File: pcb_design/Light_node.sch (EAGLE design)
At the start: 27 parts, among them IC1 ATmega328P, IC2 MIC5225-5v, Q1 reset, Y1 16MHz

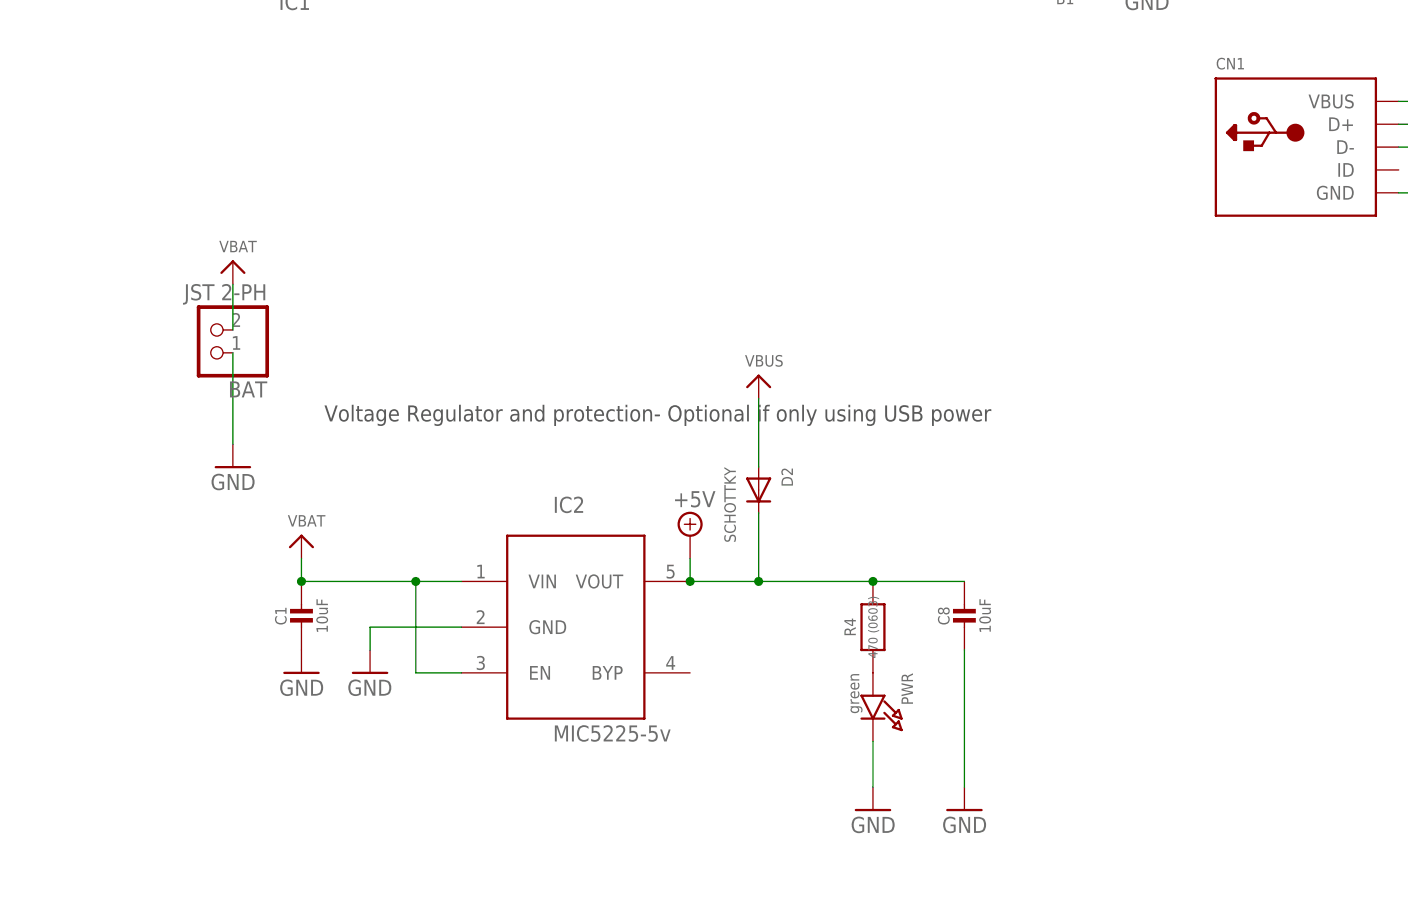
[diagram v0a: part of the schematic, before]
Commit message: Pulled the regulator components
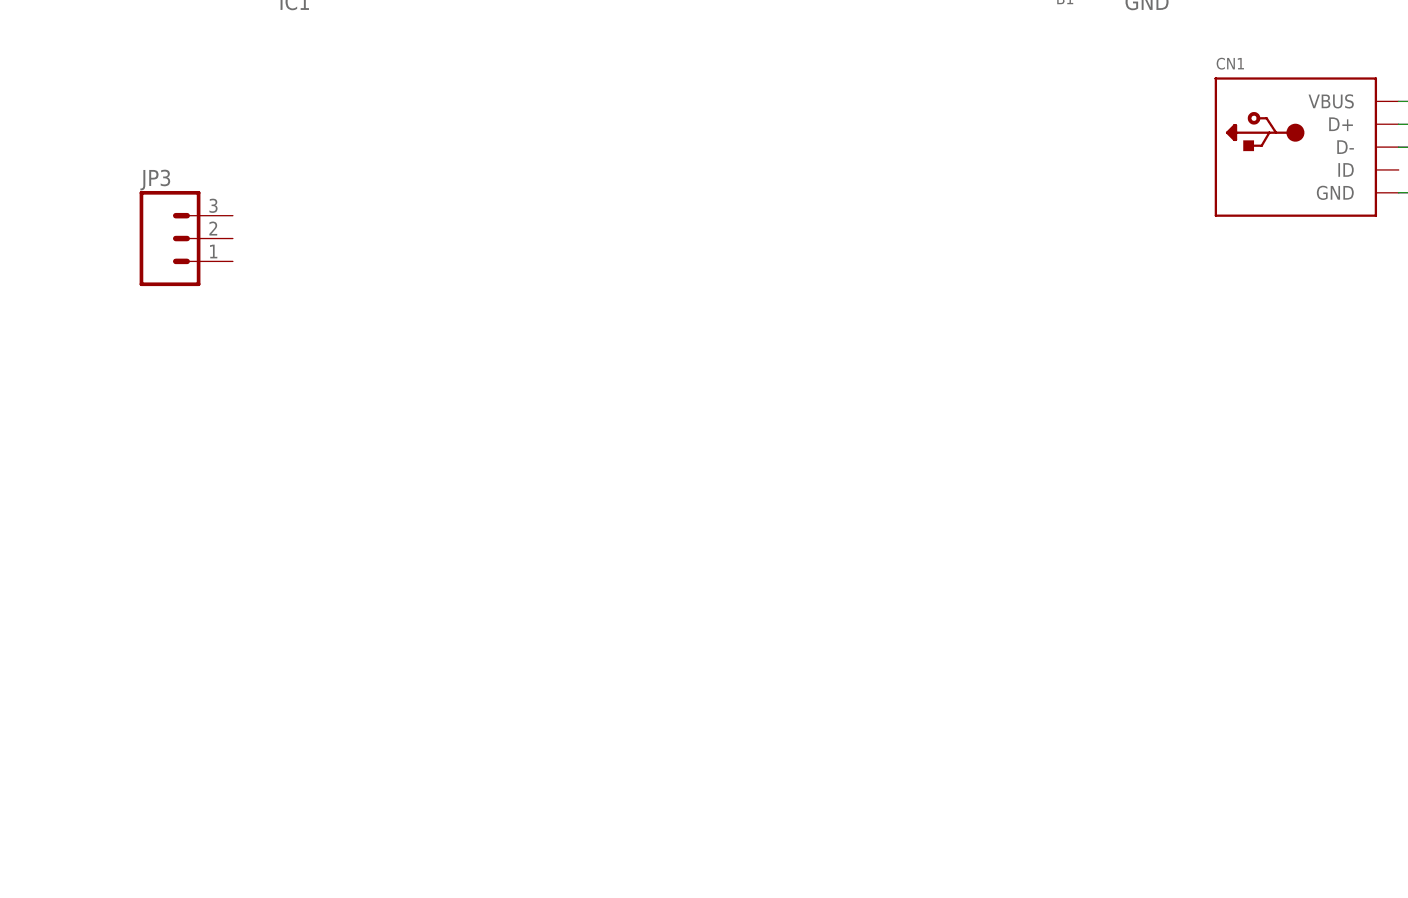
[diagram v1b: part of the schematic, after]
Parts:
- removed BAT: JST 2-PH, microbuilder:CON_JST_PH_2PIN
- removed C1, C8: 10uF, microbuilder:CAP_CERAMIC0805-NOOUTLINE
- removed D2: SCHOTTKY, adafruit:DIODE_SOD-123FL
- removed IC2: MIC5225-5v, adafruit:LP298XS
- removed PWR: green, microbuilder:LED0805_NOOUTLINE
- removed R4: 470 (0603), microbuilder:RESISTOR_0603_NOOUT
- added JP3: (no value), SparkFun:M03JST-PTH
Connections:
- removed net N$6: PWR.A, R4.1
- net +5V: no longer C8.1, D2.C, IC2.VOUT, R4.2
- net GND: no longer BAT.1, C1.2, C8.2, IC2.GND, PWR.C
- net VBAT: no longer BAT.2, C1.1, IC2.EN, IC2.VIN
- net VBUS: no longer D2.A
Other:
- note removed: "Voltage Regulator and protection- Optional if only using USB power"
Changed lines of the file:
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@@
 <part name="R2" library="microbuilder" deviceset="RESISTOR" device="_0603_NOOUT" value="68 (0603)"/>
 <part name="GND1" library="supply1" deviceset="GND" device=""/>
-<part name="GND12" library="supply1" deviceset="GND" device=""/>
 <part name="U$1" library="adafruit" deviceset="FIDUCIAL" device=""/>
 <part name="U$6" library="adafruit" deviceset="FIDUCIAL" device=""/>
 <part name="FRAME1" library="frames" deviceset="FRAME_A_L" device=""/>
-<part name="IC2" library="adafruit" deviceset="LP298X" device="S" value="MIC5225-5v"/>
-<part name="GND11" library="supply1" deviceset="GND" device=""/>
-<part name="C8" library="microbuilder" deviceset="CAP_CERAMIC" device="0805-NOOUTLINE" value="10uF"/>
 <part name="R3" library="microbuilder" deviceset="RESISTOR" device="_0603_NOOUT" value="1.5K (0603)"/>
 <part name="GND5" library="supply1" deviceset="GND" device=""/>
 <part name="Q1" library="microbuilder" deviceset="SWITCH_TACT_SMT" device="4.6X2.8" value="reset"/>
-<part name="R4" library="microbuilder" deviceset="RESISTOR" device="_0603_NOOUT" value="470 (0603)"/>
-<part name="PWR" library="microbuilder" deviceset="LED" device="0805_NOOUTLINE" value="green"/>
-<part name="GND6" library="supply1" deviceset="GND" device=""/>
-<part name="D2" library="adafruit" deviceset="DIODE" device="_SOD-123FL" value="SCHOTTKY"/>
-<part name="U$3" library="microbuilder" deviceset="VBUS" device=""/>
-<part name="U$4" library="microbuilder" deviceset="VBAT" device=""/>
-<part name="C1" library="microbuilder" deviceset="CAP_CERAMIC" device="0805-NOOUTLINE" value="10uF"/>
-<part name="GND3" library="supply1" deviceset="GND" device=""/>
 <part name="R5" library="microbuilder" deviceset="RESISTOR" device="_0603_NOOUT" value="470 (0603)"/>
 <part name="B1" library="microbuilder" deviceset="LED" device="0805_NOOUTLINE" value="red"/>
@@
 <part name="JP2" library="microbuilder" deviceset="HEADER-1X2" device="ROUND"/>
 <part name="GND13" library="supply1" deviceset="GND" device=""/>
-<part name="BAT" library="microbuilder" deviceset="CON_JST_PH_2PIN" device="" value="JST 2-PH"/>
-<part name="U$8" library="microbuilder" deviceset="VBAT" device=""/>
-<part name="GND16" library="supply1" deviceset="GND" device=""/>
 <part name="D1" library="microbuilder" deviceset="DIODE" device="SOD-323" value="3.6v"/>
 <part name="D4" library="microbuilder" deviceset="DIODE" device="SOD-323" value="3.6V"/>
@@
 <part name="GND15" library="supply1" deviceset="GND" device=""/>
 <part name="SUPPLY1" library="supply2" deviceset="+5V" device=""/>
-<part name="SUPPLY3" library="supply2" deviceset="+5V" device=""/>
 <part name="SUPPLY4" library="supply2" deviceset="+5V" device=""/>
 <part name="SUPPLY5" library="supply2" deviceset="+5V" device=""/>
 <part name="SUPPLY6" library="supply2" deviceset="+5V" device=""/>
 <part name="SUPPLY7" library="supply2" deviceset="+5V" device=""/>
+<part name="JP3" library="SparkFun" deviceset="M03" device="JST-PTH"/>
 </parts>
 <sheets>
@@
 <text x="175.26" y="25.4" size="2.54" layer="94">http://adafruit.com/products/2000</text>
 <text x="248.92" y="30.48" size="2.54" layer="94">CC 2.5 BY-SA</text>
-<text x="50.8" y="58.42" size="1.778" layer="97">Voltage Regulator and protection- Optional if only using USB power</text>
 </plain>
 <instances>
@@
 <instance part="R2" gate="G$1" x="193.04" y="86.36"/>
 <instance part="GND1" gate="1" x="177.8" y="78.74"/>
-<instance part="GND12" gate="1" x="121.92" y="15.24" rot="MR0"/>
 <instance part="U$1" gate="G$1" x="246.38" y="10.16"/>
 <instance part="U$6" gate="G$1" x="241.3" y="10.16"/>
 <instance part="FRAME1" gate="G$1" x="0" y="0"/>
 <instance part="FRAME1" gate="G$2" x="172.72" y="0"/>
-<instance part="IC2" gate="G$1" x="81.28" y="35.56" rot="R270"/>
-<instance part="GND11" gate="1" x="55.88" y="30.48"/>
-<instance part="C8" gate="G$1" x="121.92" y="35.56"/>
 <instance part="R3" gate="G$1" x="187.96" y="99.06" rot="R90"/>
 <instance part="GND5" gate="1" x="48.26" y="195.58" rot="MR270"/>
 <instance part="Q1" gate="G$1" x="40.64" y="195.58"/>
-<instance part="R4" gate="G$1" x="111.76" y="35.56" rot="R90"/>
-<instance part="PWR" gate="G$1" x="111.76" y="25.4" rot="R270"/>
-<instance part="GND6" gate="1" x="111.76" y="15.24" rot="MR0"/>
-<instance part="D2" gate="G$1" x="99.06" y="50.8" rot="R270"/>
-<instance part="U$3" gate="G$1" x="99.06" y="63.5"/>
-<instance part="U$4" gate="G$1" x="48.26" y="45.72"/>
-<instance part="C1" gate="G$1" x="48.26" y="35.56"/>
-<instance part="GND3" gate="1" x="48.26" y="30.48" rot="MR0"/>
 <instance part="R5" gate="G$1" x="124.46" y="109.22" rot="MR0"/>
 <instance part="B1" gate="G$1" x="137.16" y="109.22" rot="MR180"/>
@@
 <instance part="JP2" gate="G$1" x="104.14" y="149.86"/>
 <instance part="GND13" gate="1" x="40.64" y="119.38"/>
-<instance part="BAT" gate="G$1" x="38.1" y="68.58" rot="R180"/>
-<instance part="U$8" gate="G$1" x="40.64" y="76.2"/>
-<instance part="GND16" gate="1" x="40.64" y="53.34" rot="MR0"/>
 <instance part="D1" gate="G$1" x="182.88" y="83.82" rot="R90"/>
 <instance part="D4" gate="G$1" x="193.04" y="81.28" rot="R90"/>
@@
 <instance part="GND15" gate="1" x="193.04" y="76.2"/>
 <instance part="SUPPLY1" gate="+5V" x="22.86" y="180.34"/>
-<instance part="SUPPLY3" gate="+5V" x="91.44" y="45.72"/>
 <instance part="SUPPLY4" gate="+5V" x="187.96" y="106.68"/>
 <instance part="SUPPLY5" gate="+5V" x="33.02" y="157.48" rot="R90"/>
 <instance part="SUPPLY6" gate="+5V" x="38.1" y="129.54" rot="R90"/>
 <instance part="SUPPLY7" gate="+5V" x="157.48" y="185.42" rot="R90"/>
+<instance part="JP3" gate="G$1" x="33.02" y="78.74"/>
 </instances>
 <busses>
@@
 </segment>
 <segment>
-<wire x1="121.92" y1="17.78" x2="121.92" y2="33.02" width="0.1524" layer="91"/>
-<pinref part="GND12" gate="1" pin="GND"/>
-<pinref part="C8" gate="G$1" pin="2"/>
-</segment>
-<segment>
-<wire x1="66.04" y1="35.56" x2="55.88" y2="35.56" width="0.1524" layer="91"/>
-<wire x1="55.88" y1="35.56" x2="55.88" y2="33.02" width="0.1524" layer="91"/>
-<pinref part="GND11" gate="1" pin="GND"/>
-<pinref part="IC2" gate="G$1" pin="GND"/>
-</segment>
-<segment>
 <wire x1="45.72" y1="193.04" x2="45.72" y2="195.58" width="0.1524" layer="91"/>
 <pinref part="GND5" gate="1" pin="GND"/>
@@
 <junction x="45.72" y="195.58"/>
 <pinref part="Q1" gate="G$1" pin="S1"/>
-</segment>
-<segment>
-<pinref part="PWR" gate="G$1" pin="C"/>
-<pinref part="GND6" gate="1" pin="GND"/>
-<wire x1="111.76" y1="17.78" x2="111.76" y2="22.86" width="0.1524" layer="91"/>
-</segment>
-<segment>
-<pinref part="C1" gate="G$1" pin="2"/>
-<pinref part="GND3" gate="1" pin="GND"/>
 </segment>
 <segment>
@@
 <pinref part="IC1" gate="G$1" pin="THERMAL"/>
 <pinref part="GND13" gate="1" pin="GND"/>
-</segment>
-<segment>
-<pinref part="BAT" gate="G$1" pin="1"/>
-<pinref part="GND16" gate="1" pin="GND"/>
-<wire x1="40.64" y1="55.88" x2="40.64" y2="66.04" width="0.1524" layer="91"/>
 </segment>
 <segment>
@@
 <net name="VBUS" class="1">
 <segment>
-<pinref part="U$3" gate="G$1" pin="VBUS"/>
-<wire x1="99.06" y1="53.34" x2="99.06" y2="60.96" width="0.1524" layer="91"/>
-<pinref part="D2" gate="G$1" pin="A"/>
-</segment>
-<segment>
 <pinref part="CN1" gate="G$1" pin="VBUS"/>
 <pinref part="U$2" gate="G$1" pin="VBUS"/>
@@
 </segment>
 </net>
-<net name="N$6" class="0">
-<segment>
-<pinref part="R4" gate="G$1" pin="1"/>
-<pinref part="PWR" gate="G$1" pin="A"/>
-</segment>
-</net>
 <net name="VBAT" class="1">
-<segment>
-<pinref part="U$4" gate="G$1" pin="VBAT"/>
-<wire x1="48.26" y1="40.64" x2="48.26" y2="43.18" width="0.1524" layer="91"/>
-<wire x1="60.96" y1="40.64" x2="66.04" y2="40.64" width="0.1524" layer="91"/>
-<wire x1="66.04" y1="30.48" x2="60.96" y2="30.48" width="0.1524" layer="91"/>
-<wire x1="60.96" y1="30.48" x2="60.96" y2="40.64" width="0.1524" layer="91"/>
-<junction x="60.96" y="40.64"/>
-<pinref part="IC2" gate="G$1" pin="VIN"/>
-<pinref part="IC2" gate="G$1" pin="EN"/>
-<pinref part="C1" gate="G$1" pin="1"/>
-<junction x="48.26" y="40.64"/>
-<wire x1="48.26" y1="40.64" x2="60.96" y2="40.64" width="0.1524" layer="91"/>
-</segment>
 <segment>
 <wire x1="172.72" y1="193.04" x2="160.02" y2="193.04" width="0.1524" layer="91"/>
 <label x="160.02" y="193.04" size="1.778" layer="95"/>
 <pinref part="JP1" gate="G$1" pin="1"/>
-</segment>
-<segment>
-<pinref part="U$8" gate="G$1" pin="VBAT"/>
-<pinref part="BAT" gate="G$1" pin="2"/>
-<wire x1="40.64" y1="68.58" x2="40.64" y2="73.66" width="0.1524" layer="91"/>
 </segment>
 </net>
@@
 </segment>
 <segment>
-<pinref part="IC2" gate="G$1" pin="VOUT"/>
-<wire x1="91.44" y1="43.18" x2="91.44" y2="40.64" width="0.1524" layer="91"/>
-<wire x1="91.44" y1="40.64" x2="99.06" y2="40.64" width="0.1524" layer="91"/>
-<junction x="91.44" y="40.64"/>
-<pinref part="R4" gate="G$1" pin="2"/>
-<pinref part="C8" gate="G$1" pin="1"/>
-<wire x1="99.06" y1="40.64" x2="111.76" y2="40.64" width="0.1524" layer="91"/>
-<wire x1="111.76" y1="40.64" x2="121.92" y2="40.64" width="0.1524" layer="91"/>
-<junction x="111.76" y="40.64"/>
-<pinref part="SUPPLY3" gate="+5V" pin="+5V"/>
-<pinref part="D2" gate="G$1" pin="C"/>
-<wire x1="99.06" y1="48.26" x2="99.06" y2="40.64" width="0.1524" layer="91"/>
-<junction x="99.06" y="40.64"/>
-</segment>
-<segment>

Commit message: added a bunch of new stuff in
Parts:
- removed JP2: (no value), microbuilder:HEADER-1X2ROUND
- removed JP4: (no value), adafruit:PINHD-1X12-CB
- added B2: red, microbuilder:LED0805_NOOUTLINE
- added C1, C4: 10µF, microbuilder:CAP_CERAMIC0805-NOOUTLINE
- added C5, C8: 10uF, microbuilder:CAP_CERAMIC0805-NOOUTLINE
- added CN2: JSTPH, microbuilder:JST_2PIN
- added D2, D3: SCHOTTKY, adafruit:DIODE_SOD-123FL
- added IC2: MIC5225-3.3v, adafruit:LP298XS
- added LED2: GREEN, microbuilder:LED0805_NOOUTLINE
- added R4: 470 (0603), microbuilder:RESISTOR_0603_NOOUT
- added R8: 470, microbuilder:RESISTOR0805_NOOUTLINE
- added R9: 10K\, microbuilder:RESISTOR0805_NOOUTLINE
- added U1: MCP73831T-2ACI/OT, microbuilder:MCP73831/2
- JP1: device adafruit:PINHD-1X12-CB -> microbuilder:HEADER-1X2ROUND
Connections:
- new net +3V3: C8.1, IC2.VOUT
- new net N$10: IC1.VCC@1, IC1.VCC@2
- new net N$4: B2.A, R4.1
- new net N$5: IC1.AVCC
- new net N$6: R8.2, U1.STAT
- new net N$7: R9.1, U1.PROG
- new net N$8: LED2.A, R8.1
- new net N$9: C5.1, D2.C, D3.C, IC2.EN, IC2.VIN
- new net STRIP_CNTRL: JP3.2
- net +5V: now also C1.1, CN1.VBUS, D2.A, JP1.1, R4.2, U1.VDD; no longer IC1.AVCC, IC1.VCC@1, IC1.VCC@2, JP1.4, R6.2
- net A0: no longer JP4.7
- net A1: no longer JP4.8
- net A2: no longer JP4.9
- net A3: no longer JP4.10
- net A4: no longer JP4.11
- net A5: no longer JP4.12
- net A6: no longer JP2.1
- net A7: no longer JP2.2
- net AREF: no longer JP4.6
- net D10: no longer JP4.2
- net D11: no longer JP4.3
- net D12: no longer JP4.4
- net D13: no longer JP4.5
- net D3: no longer JP1.9
- net D4: no longer JP1.8
- net D5: no longer JP1.7
- net D6: no longer JP1.6
- net D8: no longer JP1.5
- net D9: no longer JP4.1
- net GND: now also B2.C, C1.2, C4.2, C5.2, C8.2, CN2.1, IC2.GND, JP3.1, LED2.C, R9.2, U1.VSS; no longer JP1.2
- net RESET: no longer JP1.12
- net RXD: no longer JP1.11
- net TXD: no longer JP1.10
- net VBAT: now also C4.1, CN2.2, D3.A, JP1.2, JP3.3, U1.VBAT; no longer JP1.1
- net VBUS: no longer CN1.VBUS, JP1.3
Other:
- note added: "1.0K = 1000mA"
- note added: "10K = 100mA"
- note added: "2.0K = 500mA"
- note added: "5.0K = 200mA"
- note added: "Assembly and use note : If you plan to do USB-powered operation, do not populate the Battery Charge electronics. Instead you need to solder JP1 shut"
- note added: "Battery Charger Circuit"
- note added: "USB Data and Power In"
- note added: "USB power LED"
- moved on the sheet: B1, CN1, D1, D4, R1, R2, R3, R5

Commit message: jumpe us over to using the 3.3V version of the promicro
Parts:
- removed CN2: JSTPH, microbuilder:JST_2PIN
- removed D1: 3.6v, microbuilder:DIODESOD-323
- removed D4: 3.6V, microbuilder:DIODESOD-323
- removed R8: 470, microbuilder:RESISTOR0805_NOOUTLINE
- removed R9: 10K\, microbuilder:RESISTOR0805_NOOUTLINE
- added CN3: JSTPH, microbuilder:JST_2PIN
- added JP2, JP5: (no value), microbuilder:HEADER-1X2ROUND
- added JP4: (no value), adafruit:PINHD-1X12-CB
- added PWR: green, microbuilder:LED0805_NOOUTLINE
- added R10: 470 (0603), microbuilder:RESISTOR_0603_NOOUT
- added R11: 470, microbuilder:RESISTOR0805_NOOUTLINE
- added R12: 10K\, microbuilder:RESISTOR0805_NOOUTLINE
- C1: value 10µF -> 10uF
- C5: value 10uF -> 10µF
- JP1: device microbuilder:HEADER-1X2ROUND -> adafruit:PINHD-1X12-CB
- R6: value 10K -> 10K (0603)
- Y1: value 16MHz -> 12MHz
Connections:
- removed net N$10: IC1.VCC@1, IC1.VCC@2
- net +3V3: now also IC1.AVCC, IC1.VCC@1, IC1.VCC@2, JP1.4, R3.2, R4.2, R6.2
- net +5V: now also C4.1, JP5.1, R10.2; no longer C1.1, JP1.1, R3.2, R4.2
- net A0: now also JP4.7
- net A1: now also JP4.8
- net A2: now also JP4.9
- net A3: now also JP4.10
- net A4: now also JP4.11
- net A5: now also JP4.12
- net A6: now also JP2.1
- net A7: now also JP2.2
- net AREF: now also JP4.6
- net D+: no longer D1.C
- net D-: no longer D4.C
- net D10: now also JP4.2
- net D11: now also JP4.3
- net D12: now also JP4.4
- net D13: now also JP4.5
- net D3: now also JP1.9
- net D4: now also JP1.8
- net D5: now also JP1.7
- net D6: now also JP1.6
- net D8: now also JP1.5
- net D9: now also JP4.1
- net GND: now also CN3.1, JP1.2, PWR.C, R12.2; no longer CN2.1, D1.A, D4.A, R9.2
- net N$4: now also R10.1; no longer R4.1
- net N$5: now also R11.2, U1.STAT; no longer IC1.AVCC
- net N$6: now also PWR.A, R4.1; no longer R8.2, U1.STAT
- net N$7: now also C1.1, D2.C, D3.C, IC2.EN, IC2.VIN; no longer R9.1, U1.PROG
- net N$8: now also R12.1, U1.PROG; no longer LED2.A, R8.1
- net N$9: now also LED2.A, R11.1; no longer C5.1, D2.C, D3.C, IC2.EN, IC2.VIN
- net RESET: now also JP1.12
- net RXD: now also JP1.11
- net TXD: now also JP1.10
- net VBAT: now also C5.1, CN3.2, JP1.1, JP5.2; no longer C4.1, CN2.2, JP1.2
- net VBUS: now also JP1.3
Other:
- note added: "Adafruit Pro Trinket 3.3V"
- note added: "http://adafruit.com/products/2010"
- note removed: "Adafruit Pro Trinket 5V"
- note removed: "Assembly and use note : If you plan to do USB-powered operation, do not populate the Battery Charge electronics. Instead you need to solder JP1 shut"
- note removed: "USB Data and Power In"
- note removed: "http://adafruit.com/products/2000"
- moved on the sheet: B1, B2, C1, C4, C5, C8, CN1, D2, D3, IC2, JP3, LED2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

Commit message: added in the accelerometer and removed the Reset pin
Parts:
- removed Q1: reset, microbuilder:SWITCH_TACT_SMT4.6X2.8
- added C6: 0.1uF, microbuilder:CAP_CERAMIC0805_10MGAP
- added C7: 10µF, microbuilder:CAP_CERAMIC0805-NOOUTLINE
- added JP6: (no value), microbuilder:HEADER-1X3ROUND
- added R16, R8: 10K, microbuilder:RESISTOR0805_NOOUTLINE
- added R7: TRIMPOT, SparkFun:TRIMPOT
- added U2: LIS3DHTR, microbuilder:ACCEL_LIS3DHTR
- JP2: device microbuilder:HEADER-1X2ROUND -> microbuilder:HEADER-1X870MIL
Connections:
- removed net A4: IC1.PC4(ADC4/SDA), JP4.11
- removed net A5: IC1.PC5(ADC5/SCL), JP4.12
- new net 3.3V: C6.1, C7.1, JP2.2, R8.2, U2.VDD, U2.VDDIO
- new net ADC1: JP6.1, U2.ADC1
- new net ADC2: JP6.2, U2.ADC2
- new net ADC3: JP6.3, U2.ADC3
- new net CS: JP2.7, R8.1, U2.CS
- new net INT1: JP2.8, U2.INT1
- new net SCL: IC1.PC5(ADC5/SCL), JP2.4, JP4.12, U2.SCL
- new net SDA: IC1.PC4(ADC4/SDA), JP2.5, JP4.11, U2.SDA
- new net SDO: JP2.6, R16.2, U2.SDO
- new net VIN: JP2.1
- net +3V3: now also R7.CW
- net A6: now also R7.WIPER; no longer JP2.1
- net A7: no longer JP2.2
- net GND: now also C6.2, C7.2, JP2.3, R16.1, R7.CCW, U2.GND@1, U2.GND@2, U2.RES(GND); no longer Q1.S, Q1.S1
- net RESET: no longer Q1.P, Q1.P1
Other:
- note added: "* CS needs to be set off board to select SPI or I2C"
- note added: "Bus Selection"
- note added: "CS High = I2C, Low = SPI"
- note added: "Defaults to I2C as-is (R8)"
- note added: "I2C"
- note added: "SCL (Pin 4) = Serial Clock"
- note added: "SD0 (Pin 7) = SA0/Address LSB"
- note added: "SDA (Pin 6) = Data In (MOSI)"
- note added: "SDA (Pin 6) = Serial Data"
- note added: "SDO (Pin 7) = Data Out (MISO)"
- note added: "SDO pulled low by default (R1) to set I2C address LSB to 0"
- note added: "SPI"
- note added: "Set SJ1 to make I2C"
- note added: "USB Power and Data In"
- note added: "address LSB 1"
- note added: "potentiometer for tuning stuff"
- moved on the sheet: B2, C1, C4, C5, C8, CN1, CN3, D2, D3, IC2, JP1, JP3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
